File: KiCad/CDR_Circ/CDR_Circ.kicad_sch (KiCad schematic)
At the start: 15 parts, among them U1 MPU-6050, U10 MPU-6050, U2 MPU-6050, U3 MPU-6050, U4 MPU-6050, U5 MPU-6050, U6 MPU-6050, U7 MPU-6050, U8 MPU-6050, U9 MPU-6050

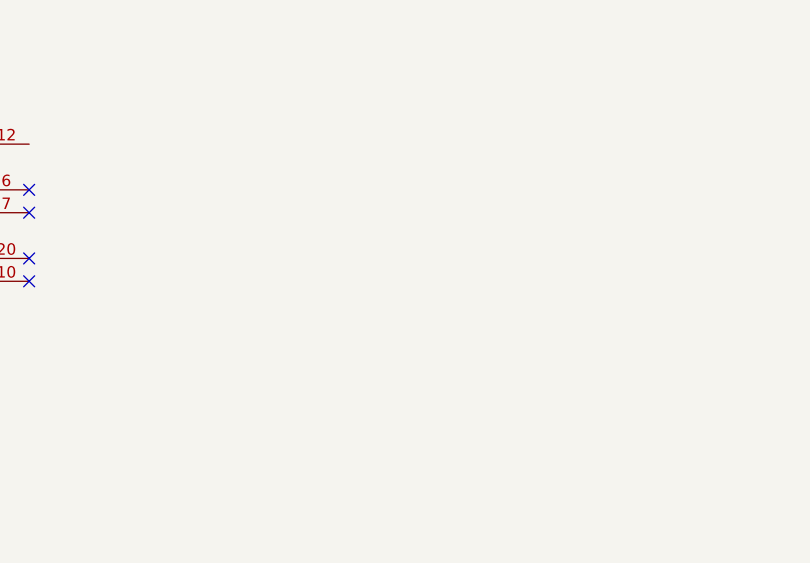
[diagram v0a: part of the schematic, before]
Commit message: include electromag
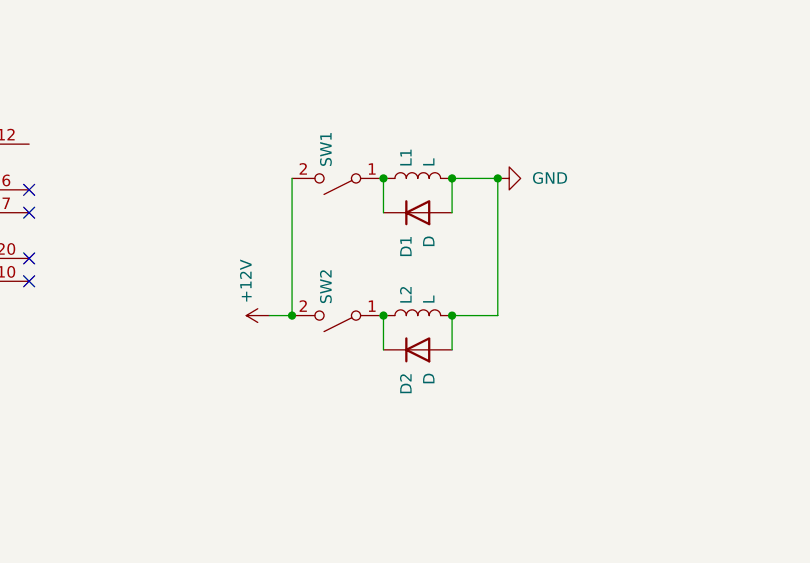
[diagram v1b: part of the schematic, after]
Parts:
- added D1, D2: D, symbol Device:D
- added L1, L2: L, symbol Device:L
- added SW1, SW2: SW_SPST, symbol Switch:SW_SPST
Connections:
- net GND: now also D1.2 (A), D2.2 (A), L1.2, L2.2
- new net: D1.1 (K), L1.1, SW1.1 (A)
- new net: D2.1 (K), L2.1, SW2.1 (A)
- new net +12V: SW1.2 (B), SW2.2 (B)

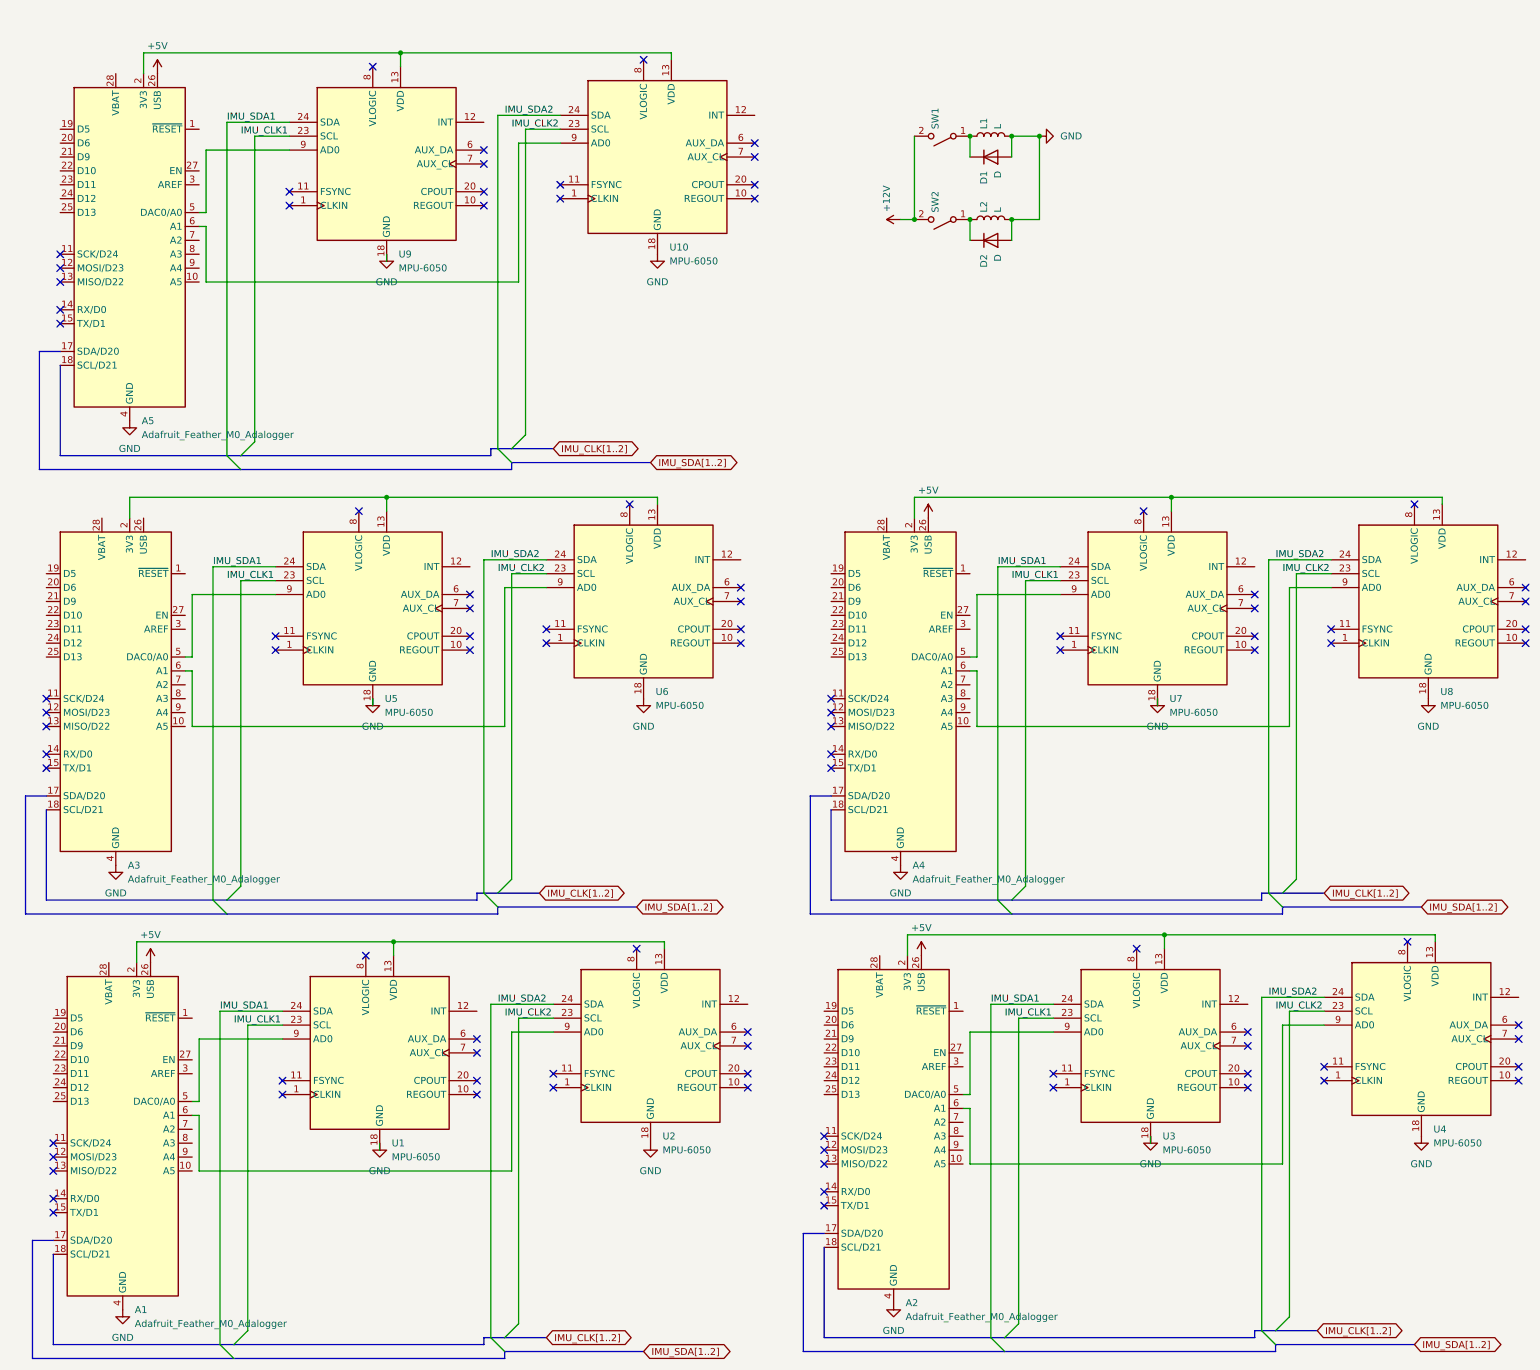
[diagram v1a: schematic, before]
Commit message: KiCad for Circuit 2.0
Added Sd card hat
Changed the amount of peripherals to 0.2
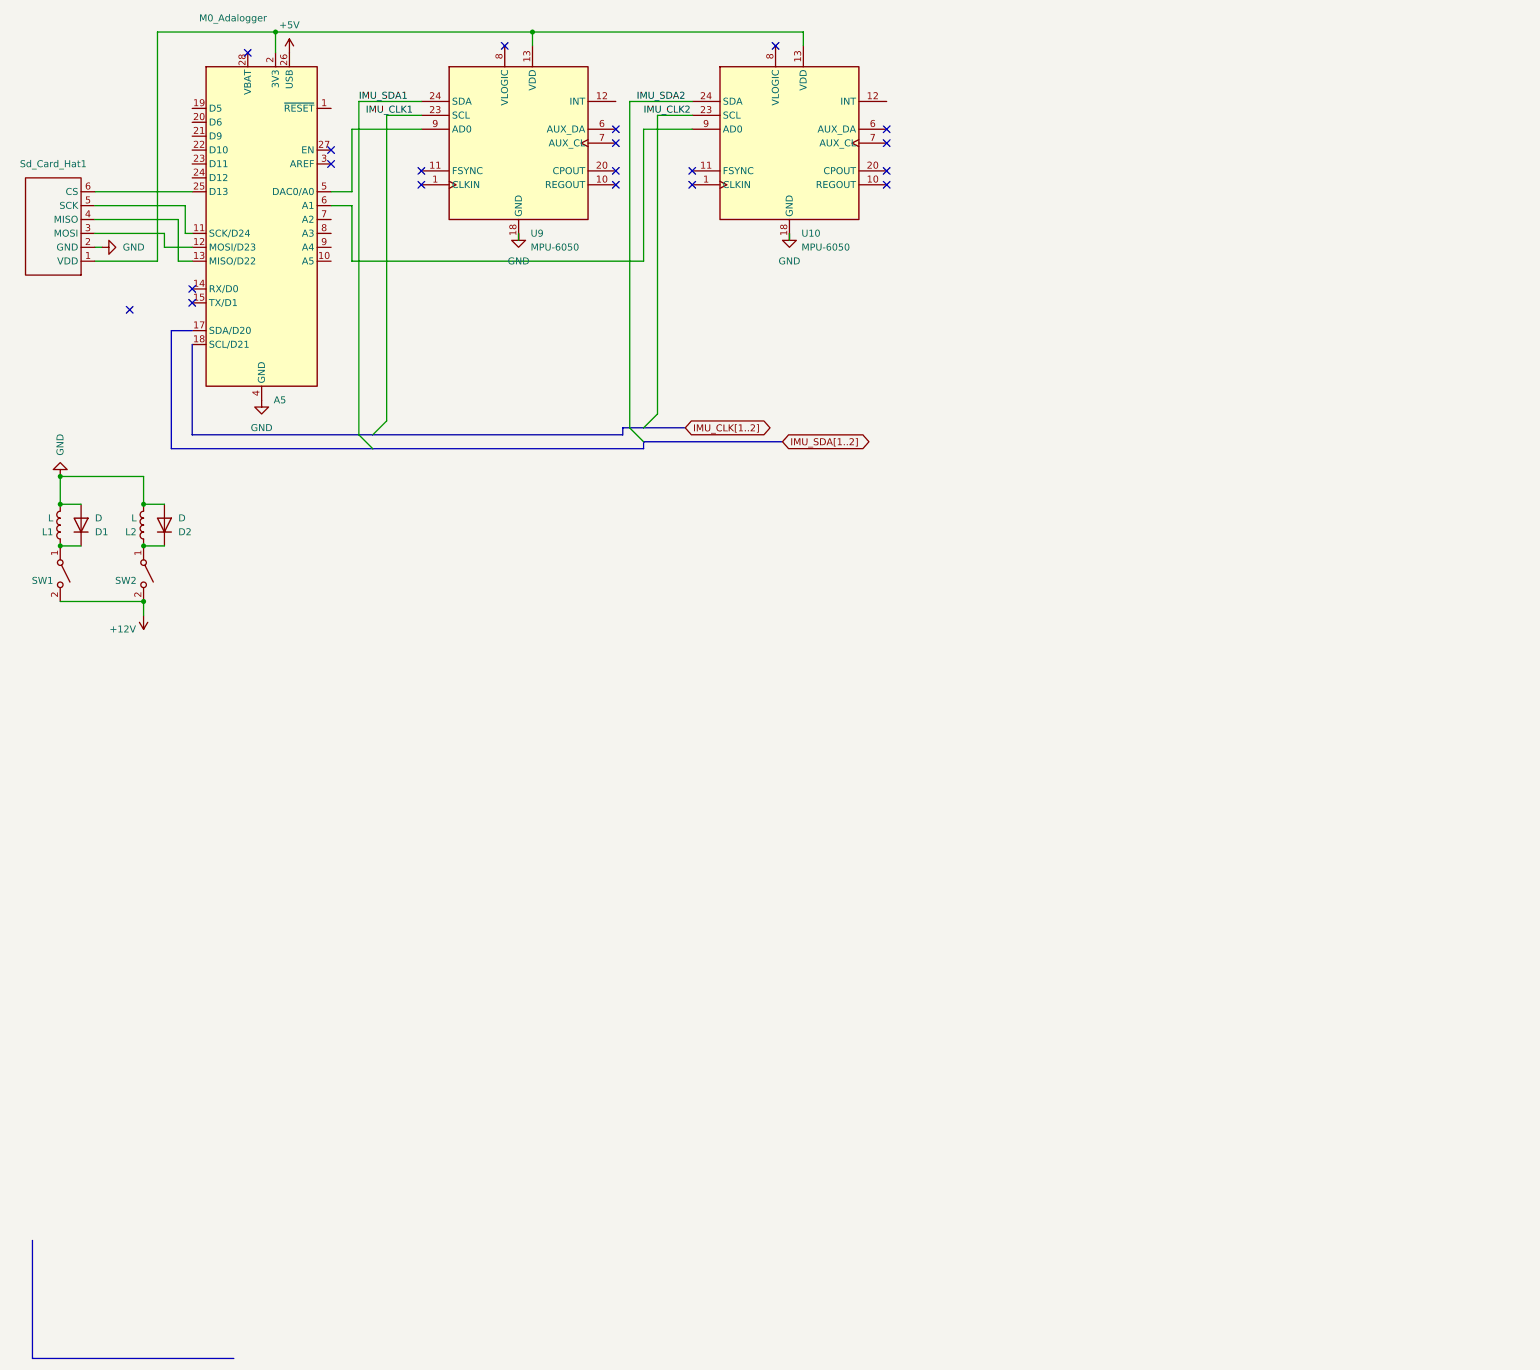
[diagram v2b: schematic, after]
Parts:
- removed A1, A2, A3, A4: Adafruit_Feather_M0_Adalogger, Module:Adafruit_Feather, symbol MCU_Module:Adafruit_Feather_M0_Adalogger
- removed U1, U2, U3, U4, U5, U6, U7, U8: MPU-6050, Sensor_Motion:InvenSense_QFN-24_4x4mm_P0.5mm, symbol Sensor_Motion:MPU-6050
- added Sd_Card_Hat1: ~, symbol New_Library:Sd_Card_Hat
- A5: value Adafruit_Feather_M0_Adalogger -> M0_Adalogger
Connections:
- net GND: now also Sd_Card_Hat1.2 (GND)
- net at A5.11 (SCK/D24): now also Sd_Card_Hat1.5 (SCK)
- net at A5.12 (MOSI/D23): now also Sd_Card_Hat1.3 (MOSI)
- net at A5.13 (MISO/D22): now also Sd_Card_Hat1.4 (MISO)
- net at A5.2 (3V3), U10.13 (VDD), U9.13 (VDD): now also Sd_Card_Hat1.1 (VDD)
- net at A5.25 (D13): now also Sd_Card_Hat1.6 (CS)
- no-connect marks 95 -> 20
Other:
- moved on the sheet: A5, D1, D2, L1, L2, SW1, SW2, U10, U9
